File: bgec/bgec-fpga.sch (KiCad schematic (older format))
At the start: 1 part

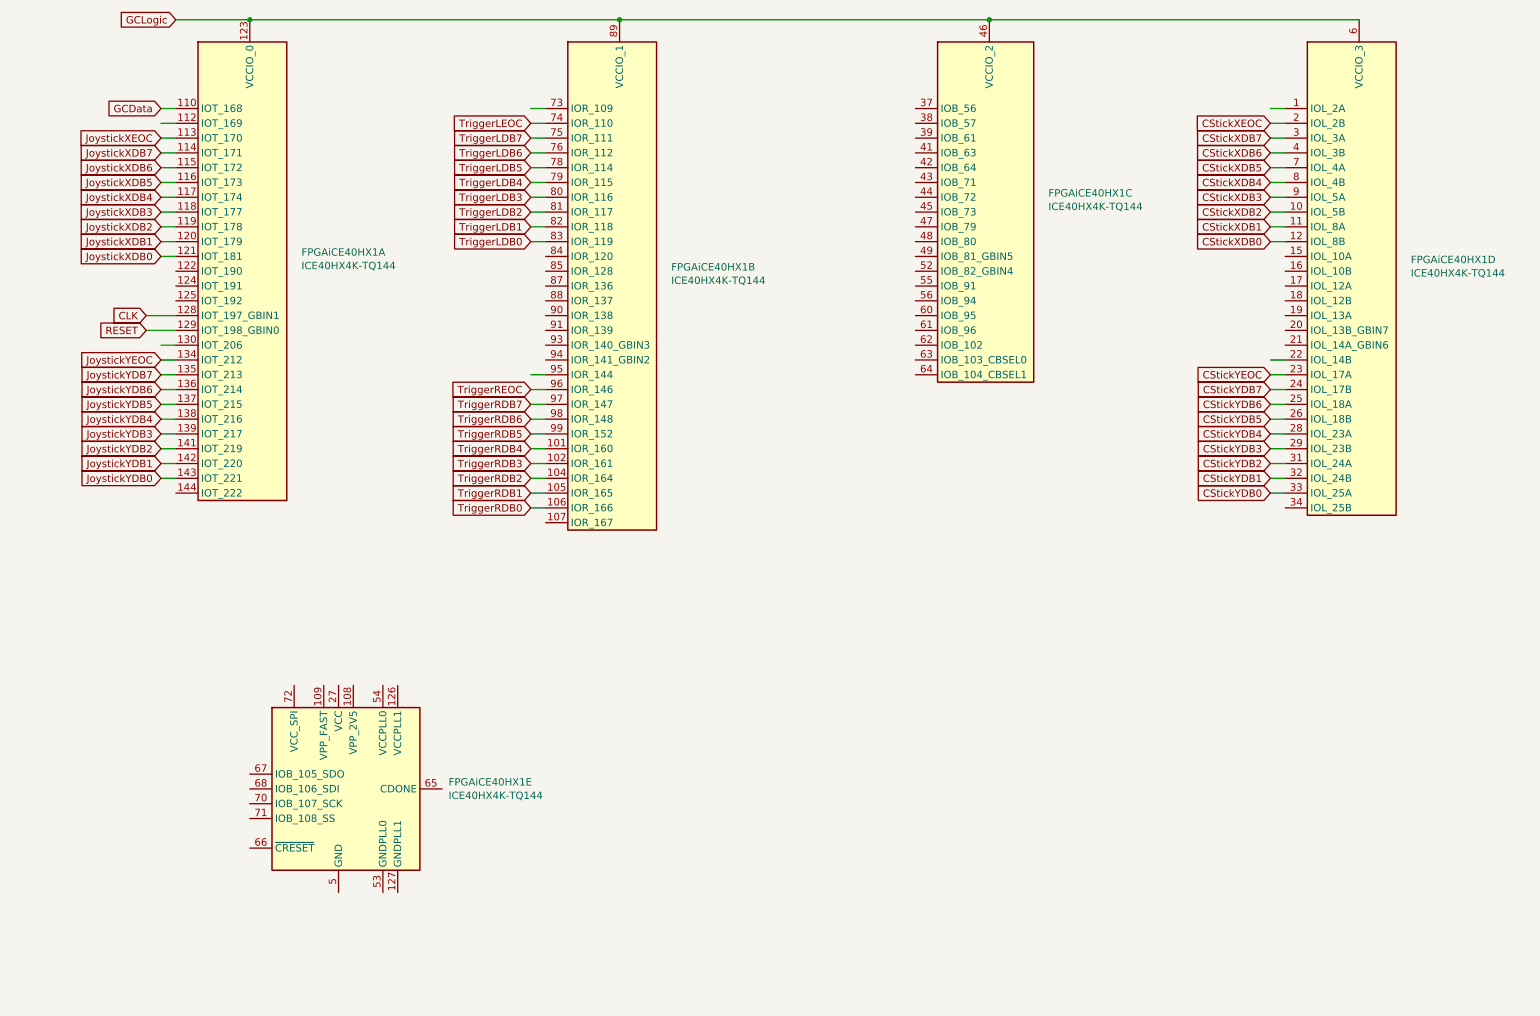
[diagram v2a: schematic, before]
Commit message: Properly feed all ADC pins to the FPGA
Includes rudimentary routing. In the future I'm definitely going to move the ADCs closer to their joysticks/triggers so the model doesn't look like a swastika.
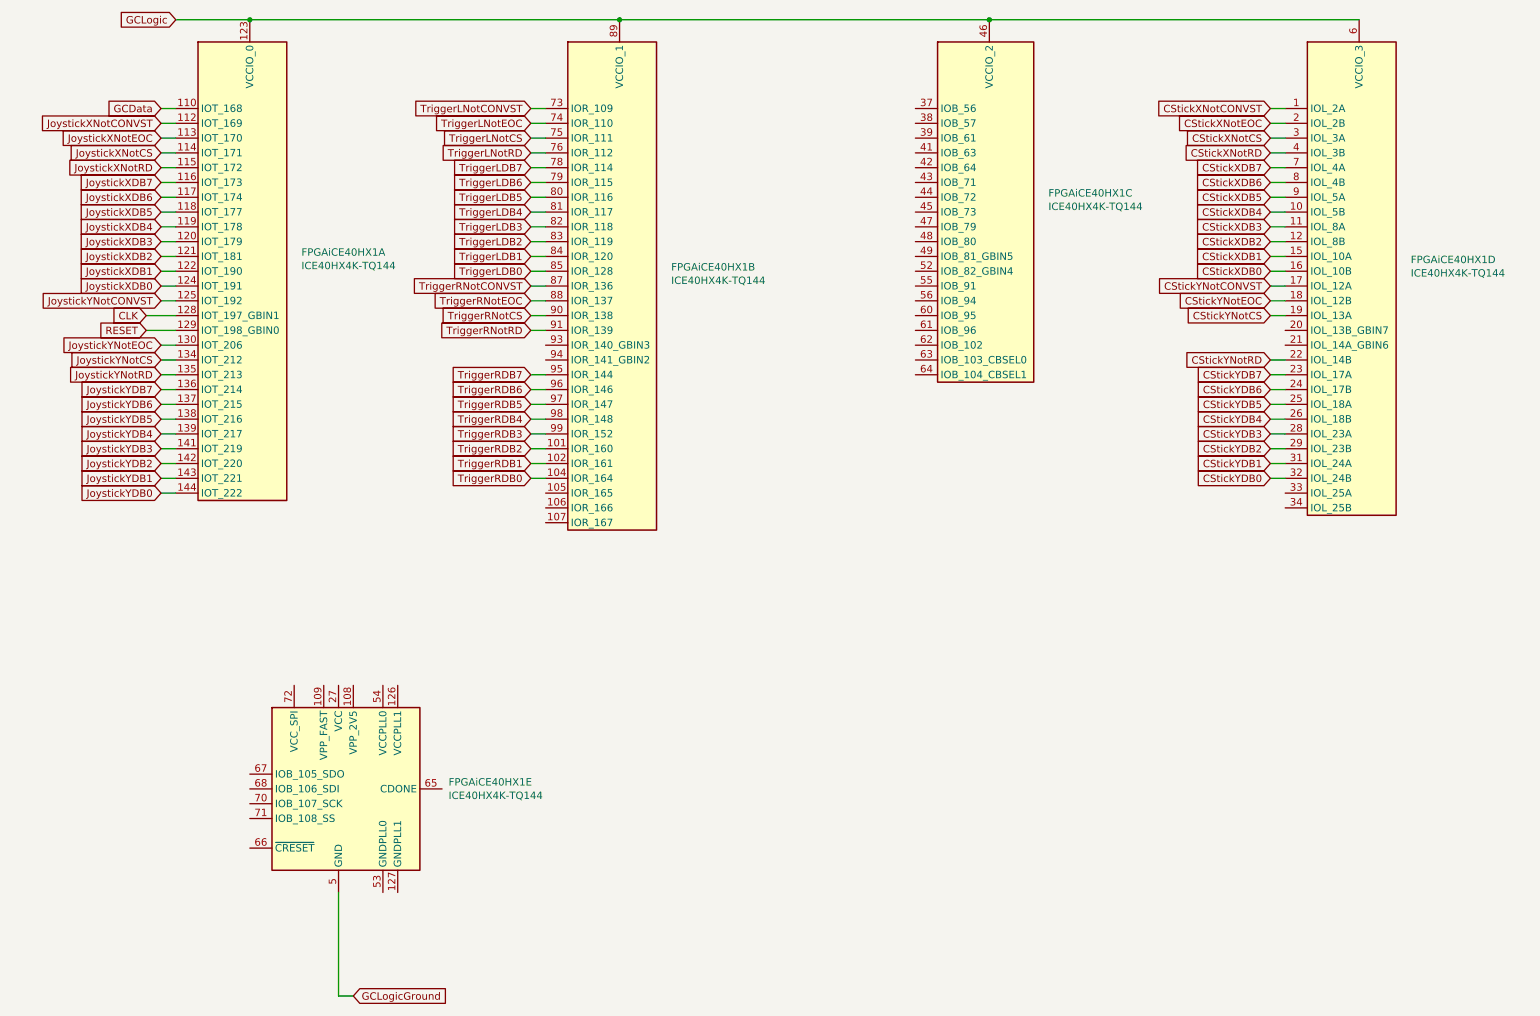
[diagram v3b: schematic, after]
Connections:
- net labels added: CStickXNotCONVST, CStickXNotCS, CStickXNotEOC, CStickXNotRD, CStickYNotCONVST, CStickYNotCS, CStickYNotEOC, CStickYNotRD, GCLogicGround, JoystickXNotCONVST, JoystickXNotCS, JoystickXNotEOC, JoystickXNotRD, JoystickYNotCONVST, JoystickYNotCS, JoystickYNotEOC, JoystickYNotRD, TriggerLNotCONVST, TriggerLNotCS, TriggerLNotEOC, TriggerLNotRD, TriggerRNotCONVST, TriggerRNotCS, TriggerRNotEOC, TriggerRNotRD
- net labels removed: CStickXEOC, CStickYEOC, JoystickXEOC, JoystickYEOC, TriggerLEOC, TriggerREOC
- wire segments 67 -> 81
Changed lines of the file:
@@
 GCLogic
 Wire Wire Line
+	4000 3700 3900 3700
+Wire Wire Line
+	3900 3800 4000 3800
+Wire Wire Line
 	4000 3900 3900 3900
 Wire Wire Line
 	3900 4000 4000 4000
 Wire Wire Line
-	4000 4100 3900 4100
-Wire Wire Line
-	3900 4200 4000 4200
-Wire Wire Line
-	3900 3800 4000 3800
-Wire Wire Line
-	4000 3700 3900 3700
-Wire Wire Line
 	3900 3600 4000 3600
 Wire Wire Line
-	3900 3500 4000 3500
+	4000 3500 3900 3500
 Wire Wire Line
 	3900 3400 4000 3400
@@
 	3900 3300 4000 3300
 Wire Wire Line
+	3900 3000 4000 3000
+Wire Wire Line
+	3900 2900 4000 2900
+Wire Wire Line
+	3900 2600 4000 2600
+Wire Wire Line
+	3900 2500 4000 2500
+Wire Wire Line
 	3900 2400 4000 2400
 Wire Wire Line
@@
 	3900 2000 4000 2000
 Wire Wire Line
-	3900 1900 4000 1900
-Wire Wire Line
-	3900 1800 4000 1800
-Wire Wire Line
-	4000 1700 3900 1700
+	4000 1900 3900 1900
 Wire Wire Line
 	3900 1600 4000 1600
@@
 	4000 1500 3900 1500
 Wire Wire Line
-	1500 4000 1400 4000
-Wire Wire Line
-	1400 3900 1500 3900
-Text GLabel 3900 4200 0    50   Input ~ 0
+	1500 4100 1400 4100
+Wire Wire Line
+	1400 4000 1500 4000
+Text GLabel 3900 4000 0    50   Input ~ 0
 TriggerRDB0
-Text GLabel 3900 4100 0    50   Input ~ 0
+Text GLabel 3900 3900 0    50   Input ~ 0
 TriggerRDB1
-Text GLabel 3900 4000 0    50   Input ~ 0
+Text GLabel 3900 3800 0    50   Input ~ 0
 TriggerRDB2
-Text GLabel 3900 3900 0    50   Input ~ 0
+Text GLabel 3900 3700 0    50   Input ~ 0
 TriggerRDB3
-Text GLabel 3900 3800 0    50   Input ~ 0
+Text GLabel 3900 3600 0    50   Input ~ 0
 TriggerRDB4
-Text GLabel 3900 3700 0    50   Input ~ 0
+Text GLabel 3900 3500 0    50   Input ~ 0
 TriggerRDB5
-Text GLabel 3900 3600 0    50   Input ~ 0
+Text GLabel 3900 3400 0    50   Input ~ 0
 TriggerRDB6
-Text GLabel 3900 3500 0    50   Input ~ 0
+Text GLabel 3900 3300 0    50   Input ~ 0
 TriggerRDB7
-Text GLabel 3900 3400 0    50   Input ~ 0
-TriggerREOC
+Text GLabel 3900 2800 0    50   Input ~ 0
+TriggerRNotEOC
+Text GLabel 3900 2600 0    50   Input ~ 0
+TriggerLDB0
+Text GLabel 3900 2500 0    50   Input ~ 0
+TriggerLDB1
 Text GLabel 3900 2400 0    50   Input ~ 0
-TriggerLDB0
+TriggerLDB2
 Text GLabel 3900 2300 0    50   Input ~ 0
-TriggerLDB1
+TriggerLDB3
 Text GLabel 3900 2200 0    50   Input ~ 0
-TriggerLDB2
+TriggerLDB4
 Text GLabel 3900 2100 0    50   Input ~ 0
-TriggerLDB3
+TriggerLDB5
 Text GLabel 3900 2000 0    50   Input ~ 0
-TriggerLDB4
+TriggerLDB6
 Text GLabel 3900 1900 0    50   Input ~ 0
-TriggerLDB5
-Text GLabel 3900 1800 0    50   Input ~ 0
-TriggerLDB6
-Text GLabel 3900 1700 0    50   Input ~ 0
 TriggerLDB7
 Text GLabel 3900 1600 0    50   Input ~ 0
-TriggerLEOC
+TriggerLNotEOC
 Wire Wire Line
 	1400 1500 1500 1500
@@
 GCData
 Wire Wire Line
+	1400 3900 1500 3900
+Wire Wire Line
 	1400 3800 1500 3800
 Wire Wire Line
@@
 	1400 3400 1500 3400
 Wire Wire Line
-	1400 3300 1500 3300
-Wire Wire Line
 	1400 3200 1500 3200
 Wire Wire Line
 	1400 3100 1500 3100
 Wire Wire Line
-	1400 2500 1500 2500
-Text GLabel 1400 3300 0    50   Input ~ 0
+	1400 2700 1500 2700
+Text GLabel 1400 3400 0    50   Input ~ 0
 JoystickYDB7
-Text GLabel 1400 3400 0    50   Input ~ 0
+Text GLabel 1400 3500 0    50   Input ~ 0
 JoystickYDB6
-Text GLabel 1400 3500 0    50   Input ~ 0
+Text GLabel 1400 3600 0    50   Input ~ 0
 JoystickYDB5
-Text GLabel 1400 3600 0    50   Input ~ 0
+Text GLabel 1400 3700 0    50   Input ~ 0
 JoystickYDB4
-Text GLabel 1400 3700 0    50   Input ~ 0
+Text GLabel 1400 3800 0    50   Input ~ 0
 JoystickYDB3
-Text GLabel 1400 3800 0    50   Input ~ 0
+Text GLabel 1400 3900 0    50   Input ~ 0
 JoystickYDB2
-Text GLabel 1400 3900 0    50   Input ~ 0
+Text GLabel 1400 4000 0    50   Input ~ 0
 JoystickYDB1
-Text GLabel 1400 4000 0    50   Input ~ 0
+Text GLabel 1400 4100 0    50   Input ~ 0
 JoystickYDB0
-Text GLabel 1400 3200 0    50   Input ~ 0
-JoystickYEOC
+Text GLabel 1400 3100 0    50   Input ~ 0
+JoystickYNotEOC
+Wire Wire Line
+	1400 2600 1500 2600
+Wire Wire Line
+	1500 2500 1400 2500
 Wire Wire Line
 	1400 2400 1500 2400
@@
 	1400 2000 1500 2000
 Wire Wire Line
-	1500 1900 1400 1900
-Wire Wire Line
-	1400 1800 1500 1800
-Wire Wire Line
 	1500 1700 1400 1700
 Wire Wire Line
 	1400 1600 1500 1600
-Text GLabel 1400 1800 0    50   Input ~ 0
+Text GLabel 1400 2000 0    50   Input ~ 0
 JoystickXDB7
-Text GLabel 1400 1900 0    50   Input ~ 0
+Text GLabel 1400 2100 0    50   Input ~ 0
 JoystickXDB6
-Text GLabel 1400 2000 0    50   Input ~ 0
+Text GLabel 1400 2200 0    50   Input ~ 0
 JoystickXDB5
-Text GLabel 1400 2100 0    50   Input ~ 0
+Text GLabel 1400 2300 0    50   Input ~ 0
 JoystickXDB4
-Text GLabel 1400 2200 0    50   Input ~ 0
+Text GLabel 1400 2400 0    50   Input ~ 0
 JoystickXDB3
-Text GLabel 1400 2300 0    50   Input ~ 0
+Text GLabel 1400 2500 0    50   Input ~ 0
 JoystickXDB2
-Text GLabel 1400 2400 0    50   Input ~ 0
+Text GLabel 1400 2600 0    50   Input ~ 0
 JoystickXDB1
-Text GLabel 1400 2500 0    50   Input ~ 0
+Text GLabel 1400 2700 0    50   Input ~ 0
 JoystickXDB0
 Text GLabel 1400 1700 0    50   Input ~ 0
-JoystickXEOC
+JoystickXNotEOC
 Wire Wire Line
 	1300 3000 1500 3000
@@
 Connection ~ 7000 900
 Wire Wire Line
+	8900 2600 9000 2600
+Wire Wire Line
+	8900 2500 9000 2500
+Wire Wire Line
 	8900 2400 9000 2400
 Wire Wire Line
@@
 	8900 2000 9000 2000
 Wire Wire Line
-	8900 1900 9000 1900
-Wire Wire Line
-	8900 1800 9000 1800
-Wire Wire Line
-	9000 1700 8900 1700
+	9000 1900 8900 1900
 Wire Wire Line
 	8900 1600 9000 1600
 Wire Wire Line
 	9000 1500 8900 1500
+Text GLabel 8900 2600 0    50   Input ~ 0
+CStickXDB0
+Text GLabel 8900 2500 0    50   Input ~ 0
+CStickXDB1
 Text GLabel 8900 2400 0    50   Input ~ 0
-CStickXDB0
+CStickXDB2
 Text GLabel 8900 2300 0    50   Input ~ 0
-CStickXDB1
+CStickXDB3
 Text GLabel 8900 2200 0    50   Input ~ 0
-CStickXDB2
+CStickXDB4
 Text GLabel 8900 2100 0    50   Input ~ 0
-CStickXDB3
+CStickXDB5
 Text GLabel 8900 2000 0    50   Input ~ 0
-CStickXDB4
+CStickXDB6
 Text GLabel 8900 1900 0    50   Input ~ 0
-CStickXDB5
-Text GLabel 8900 1800 0    50   Input ~ 0
-CStickXDB6
-Text GLabel 8900 1700 0    50   Input ~ 0
 CStickXDB7
 Text GLabel 8900 1600 0    50   Input ~ 0
-CStickXEOC
-Wire Wire Line
-	8900 4100 9000 4100
+CStickXNotEOC
 Wire Wire Line
 	8900 4000 9000 4000
@@
 	8900 3500 9000 3500
 Wire Wire Line
-	9000 3400 8900 3400
-Wire Wire Line
-	8900 3300 9000 3300
-Wire Wire Line
-	9000 3200 8900 3200
-Text GLabel 8900 4100 0    50   Input ~ 0
+	8900 3400 9000 3400
+Wire Wire Line
+	9000 3300 8900 3300
+Wire Wire Line
+	8900 2800 9000 2800
+Wire Wire Line
+	9000 2700 8900 2700
+Text GLabel 8900 4000 0    50   Input ~ 0
 CStickYDB0
-Text GLabel 8900 4000 0    50   Input ~ 0
+Text GLabel 8900 3900 0    50   Input ~ 0
 CStickYDB1
-Text GLabel 8900 3900 0    50   Input ~ 0
+Text GLabel 8900 3800 0    50   Input ~ 0
 CStickYDB2
-Text GLabel 8900 3800 0    50   Input ~ 0
+Text GLabel 8900 3700 0    50   Input ~ 0
 CStickYDB3
-Text GLabel 8900 3700 0    50   Input ~ 0
+Text GLabel 8900 3600 0    50   Input ~ 0
 CStickYDB4
-Text GLabel 8900 3600 0    50   Input ~ 0
+Text GLabel 8900 3500 0    50   Input ~ 0
 CStickYDB5
-Text GLabel 8900 3500 0    50   Input ~ 0
+Text GLabel 8900 3400 0    50   Input ~ 0
 CStickYDB6
-Text GLabel 8900 3400 0    50   Input ~ 0
+Text GLabel 8900 3300 0    50   Input ~ 0
 CStickYDB7
-Text GLabel 8900 3300 0    50   Input ~ 0
-CStickYEOC
+Text GLabel 8900 2800 0    50   Input ~ 0
+CStickYNotEOC
+Text GLabel 1400 1600 0    50   Input ~ 0
+JoystickXNotCONVST
+Text GLabel 1400 1800 0    50   Input ~ 0
+JoystickXNotCS
+Text GLabel 1400 1900 0    50   Input ~ 0
+JoystickXNotRD
+Wire Wire Line
+	1400 1800 1500 1800
+Wire Wire Line
+	1400 1900 1500 1900
+Text GLabel 1400 2800 0    50   Input ~ 0
+JoystickYNotCONVST
+Text GLabel 1400 3200 0    50   Input ~ 0
+JoystickYNotCS
+Text GLabel 1400 3300 0    50   Input ~ 0
+JoystickYNotRD
+Wire Wire Line
+	1400 2800 1500 2800
+Wire Wire Line
+	1400 3300 1500 3300
+Text GLabel 3900 1500 0    50   Input ~ 0
+TriggerLNotCONVST
+Text GLabel 3900 1700 0    50   Input ~ 0
+TriggerLNotCS
+Text GLabel 3900 1800 0    50   Input ~ 0
+TriggerLNotRD
+Wire Wire Line
+	3900 1700 4000 1700
+Wire Wire Line
+	3900 1800 4000 1800
+Text GLabel 3900 2700 0    50   Input ~ 0
+TriggerRNotCONVST
+Text GLabel 3900 2900 0    50   Input ~ 0
+TriggerRNotCS
+Text GLabel 3900 3000 0    50   Input ~ 0
+TriggerRNotRD
+Wire Wire Line
+	3900 2800 4000 2800
+Wire Wire Line
+	3900 2700 4000 2700
+Text GLabel 8900 2700 0    50   Input ~ 0
+CStickYNotCONVST
+Text GLabel 8900 2900 0    50   Input ~ 0
+CStickYNotCS
+Text GLabel 8900 3200 0    50   Input ~ 0
+CStickYNotRD
+Text GLabel 8900 1500 0    50   Input ~ 0
+CStickXNotCONVST
+Text GLabel 8900 1700 0    50   Input ~ 0
+CStickXNotCS
+Text GLabel 8900 1800 0    50   Input ~ 0
+CStickXNotRD
+Wire Wire Line
+	8900 1700 9000 1700
+Wire Wire Line
+	9000 1800 8900 1800
+Wire Wire Line
+	8900 2900 9000 2900
+Wire Wire Line
+	8900 3200 9000 3200
+Text GLabel 2700 7500 2    50   Input ~ 0
+GCLogicGround
+Wire Wire Line
+	2600 6800 2600 7500
+Wire Wire Line
+	2600 7500 2700 7500
 $EndSCHEMATC

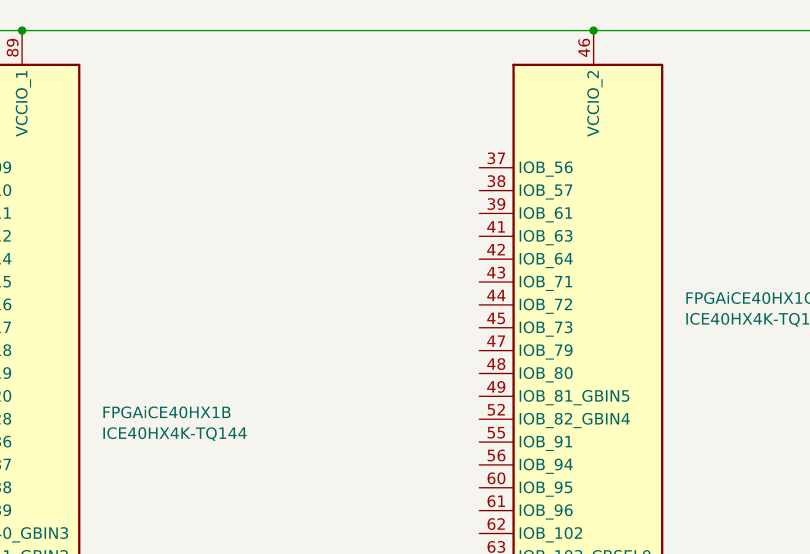
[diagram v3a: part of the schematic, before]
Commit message: Remodel ADC placement, add USB-C connector
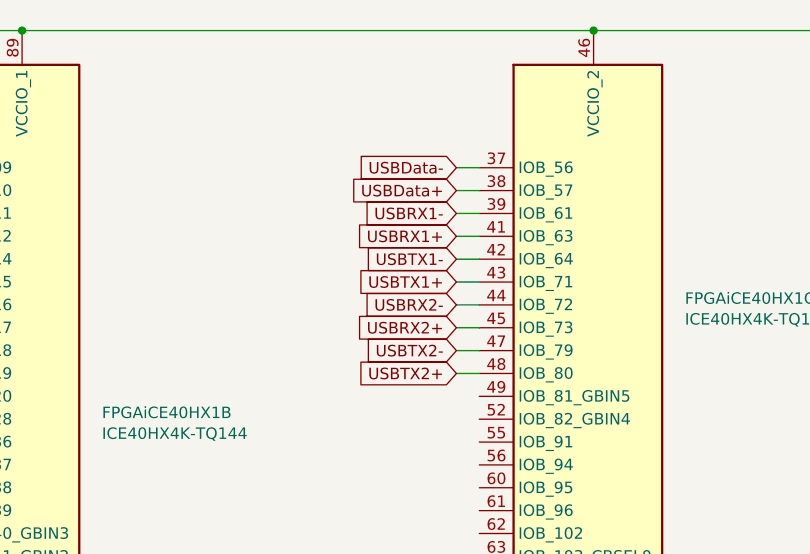
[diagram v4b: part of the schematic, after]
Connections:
- net USBData-: now reaches FPGAiCE40HX1.37 (IOB_56)
- net USBData+: now reaches FPGAiCE40HX1.38 (IOB_57)
- net USBRX1-: now reaches FPGAiCE40HX1.39 (IOB_61)
- net USBRX1+: now reaches FPGAiCE40HX1.41 (IOB_63)
- net USBTX1-: now reaches FPGAiCE40HX1.42 (IOB_64)
- net USBTX1+: now reaches FPGAiCE40HX1.43 (IOB_71)
- net USBRX2-: now reaches FPGAiCE40HX1.44 (IOB_72)
- net USBRX2+: now reaches FPGAiCE40HX1.45 (IOB_73)
- net USBTX2-: now reaches FPGAiCE40HX1.47 (IOB_79)
- net USBTX2+: now reaches FPGAiCE40HX1.48 (IOB_80)
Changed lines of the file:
@@
 $Descr A4 11693 8268
 encoding utf-8
-Sheet 2 3
+Sheet 2 4
 Title ""
 Date ""
@@
 Wire Wire Line
 	2600 7500 2700 7500
+Text GLabel 6400 1500 0    50   Input ~ 0
+USBData-
+Text GLabel 6400 1600 0    50   Input ~ 0
+USBData+
+Wire Wire Line
+	6400 1500 6500 1500
+Wire Wire Line
+	6400 1600 6500 1600
+Text GLabel 6400 1700 0    50   Input ~ 0
+USBRX1-
+Text GLabel 6400 1800 0    50   Input ~ 0
+USBRX1+
+Text GLabel 6400 1900 0    50   Input ~ 0
+USBTX1-
+Text GLabel 6400 2000 0    50   Input ~ 0
+USBTX1+
+Text GLabel 6400 2100 0    50   Input ~ 0
+USBRX2-
+Text GLabel 6400 2200 0    50   Input ~ 0
+USBRX2+
+Text GLabel 6400 2300 0    50   Input ~ 0
+USBTX2-
+Text GLabel 6400 2400 0    50   Input ~ 0
+USBTX2+
+Wire Wire Line
+	6400 1700 6500 1700
+Wire Wire Line
+	6400 1800 6500 1800
+Wire Wire Line
+	6400 1900 6500 1900
+Wire Wire Line
+	6400 2000 6500 2000
+Wire Wire Line
+	6400 2100 6500 2100
+Wire Wire Line
+	6400 2200 6500 2200
+Wire Wire Line
+	6400 2300 6500 2300
+Wire Wire Line
+	6400 2400 6500 2400
 $EndSCHEMATC
